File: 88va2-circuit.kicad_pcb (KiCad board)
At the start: 4 copper layers, 380 x 237.5 mm, 41 parts, among them CN2 FDD, CN4 TEXT BUS, CN5 LED, IC1 D65101GD055, IC13 SN74ALS374N, IC20 7407, IC21 uPD4990AC, IC22 DIP-14_W7.62mm, IC65 D65101GD110, IC9 D65200GD076, X2 32.768K

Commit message: wire power lines
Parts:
- added REF**: R_Array_SIP9, Resistor_THT:R_Array_SIP9, F.Cu at (83.5, 27.9)
- moved R18 2.35 mm to (98.7, 24.1)
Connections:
- IC1 pad 1: (no net) -> +5V
- IC1 pad 40: (no net) -> +5V
- IC1 pad 41: (no net) -> GND
- IC1 pad 42: (no net) -> GND
- IC1 pad 80: GND -> (no net)
- IC1 pad 81: +5V -> (no net)
- IC9 pad 1: (no net) -> +5V
- IC9 pad 41: (no net) -> GND
- IC9 pad 42: (no net) -> GND
- IC9 pad 79: GND -> (no net)
- IC9 pad 80: GND -> (no net)
- IC9 pad 81: +5V -> (no net)
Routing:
- net +5V: track 856.7 -> 1129.3 mm, vias 3 -> 6
- net GND: track 1260.7 -> 1372.7 mm, vias 10 -> 12
- net Net-(IC13-8D): track 54.2 -> 51.9 mm

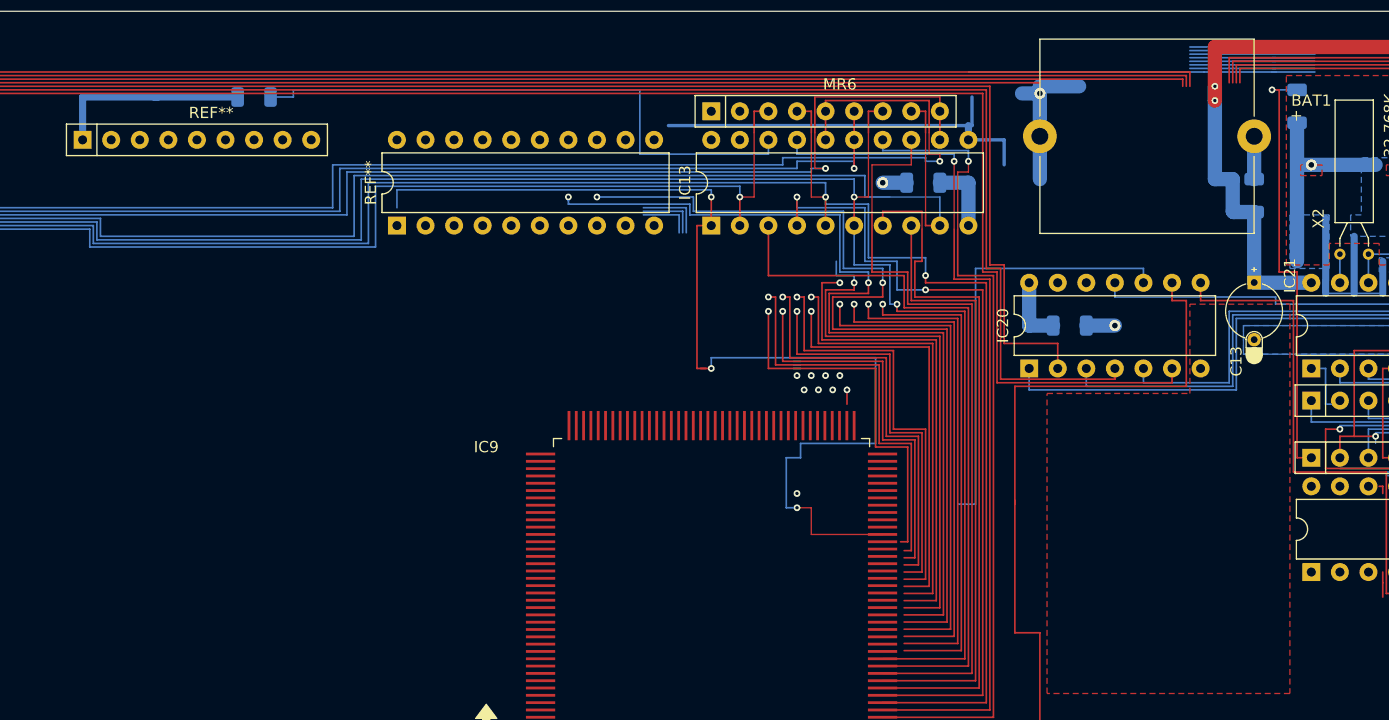
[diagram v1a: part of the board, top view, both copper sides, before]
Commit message: wire IC8, MR3
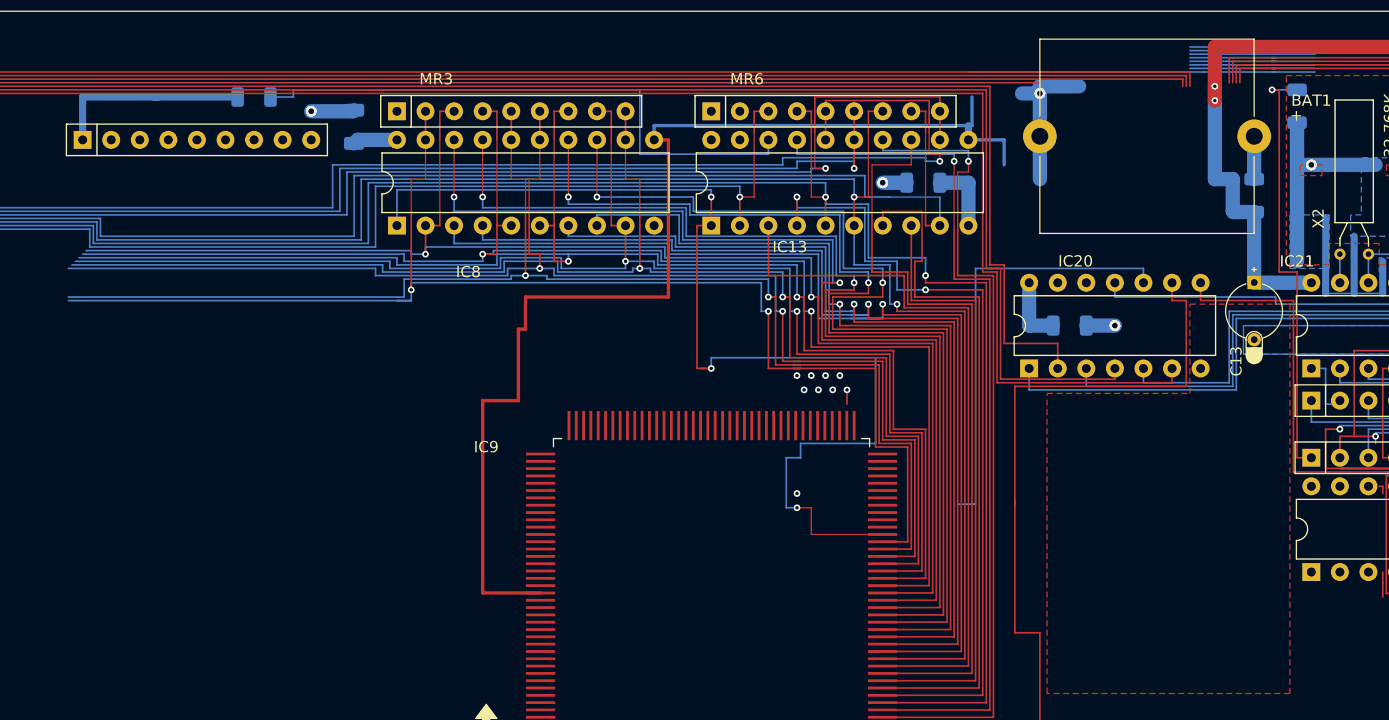
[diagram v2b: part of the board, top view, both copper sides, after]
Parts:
- removed the REF** at (111.4, 35.5)
- added C44: C_Small, Capacitor_SMD:C_1206_3216Metric, B.Cu at (107.6, 26.8)
- added IC8: SN74ALS374N, Package_DIP:DIP-20_W7.62mm, F.Cu at (111.4, 35.5)
- added MR3: 33kΩ, Resistor_THT:R_Array_SIP9, F.Cu at (111.4, 25.4)
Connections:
- IC9 pad 53: (no net) -> Net-(IC8-1D)
- IC9 pad 54: (no net) -> Net-(IC8-2D)
- IC9 pad 55: (no net) -> Net-(IC8-3D)
- IC9 pad 56: (no net) -> Net-(IC8-4D)
- IC9 pad 57: (no net) -> Net-(IC8-5D)
- IC9 pad 58: (no net) -> Net-(IC8-6D)
- IC9 pad 59: (no net) -> Net-(IC8-7D)
- IC9 pad 60: (no net) -> Net-(IC8-8D)
- IC9 pad 61: (no net) -> SCLK0
- IC9 pad 62: (no net) -> SCLK1
- IC9 pad 63: (no net) -> SCLK2
- IC9 pad 64: (no net) -> SCLK3
- IC9 pad 65: (no net) -> SCLK4
- IC9 pad 66: (no net) -> SCLK5
- IC9 pad 67: (no net) -> SCLK6
- IC9 pad 68: (no net) -> SCLK7
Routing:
- net (no net): track 2451.6 -> 1717.7 mm, vias 60 -> 42
- net SCLK1: track 0.00 -> 127.3 mm, vias 0 -> 2
- net SCLK2: track 0.00 -> 127.3 mm, vias 0 -> 2
- net SCLK0: track 0.00 -> 126.7 mm, vias 0 -> 2
- net SCLK3: track 0.00 -> 125.3 mm, vias 0 -> 2
- net SCLK4: track 0.00 -> 122.8 mm, vias 0 -> 2
- net SCLK5: track 0.00 -> 120.9 mm, vias 0 -> 2
- net SCLK7: track 0.00 -> 119.9 mm, vias 0 -> 2
- net SCLK6: track 0.00 -> 119.6 mm, vias 0 -> 2
- net Net-(IC8-1D): track 0.00 -> 95.3 mm, vias 0 -> 1
- net Net-(IC8-7D): track 0.00 -> 92.4 mm, vias 0 -> 2
- net Net-(IC8-8D): track 0.00 -> 91.7 mm, vias 0 -> 2
- net Net-(IC8-2D): track 0.00 -> 89.6 mm, vias 0 -> 1
- net Net-(IC8-5D): track 0.00 -> 88.6 mm, vias 0 -> 2
- net Net-(IC8-6D): track 0.00 -> 88.3 mm, vias 0 -> 2
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
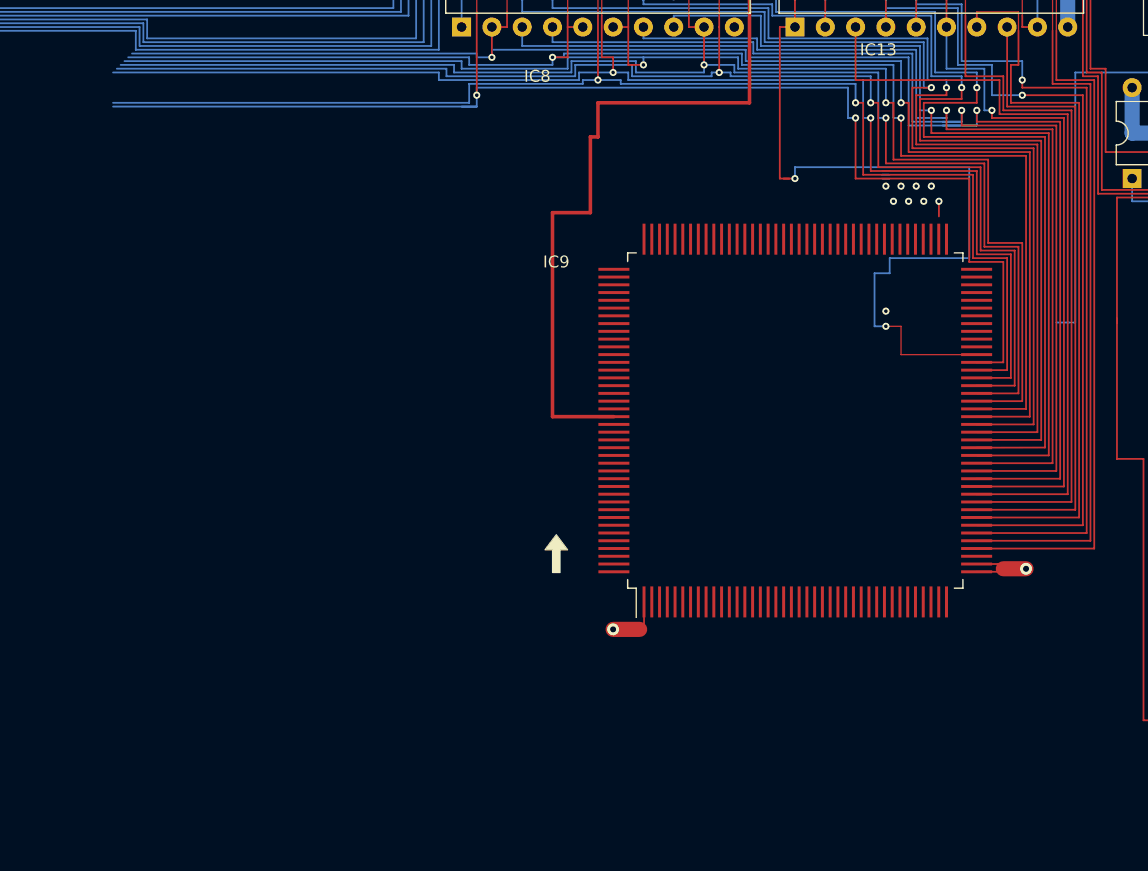
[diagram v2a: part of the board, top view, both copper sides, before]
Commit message: wire IC13/IC8 CLK
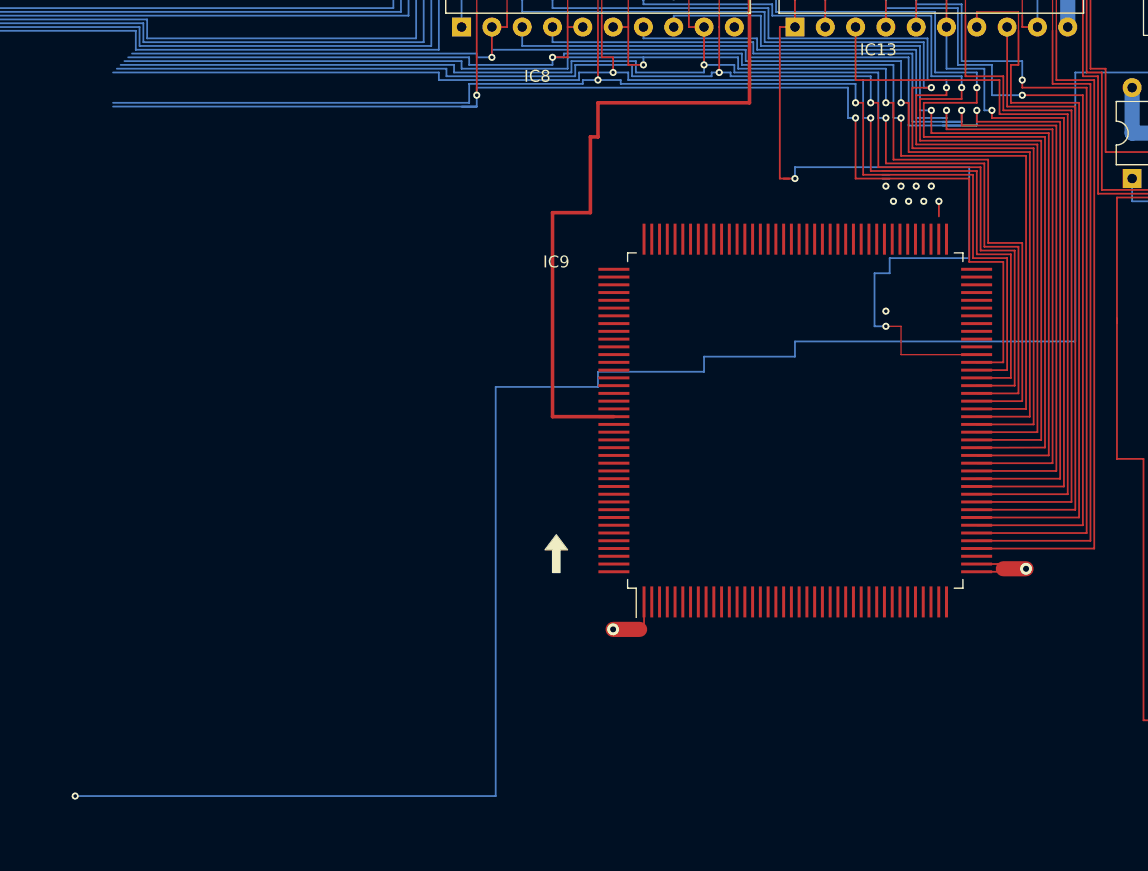
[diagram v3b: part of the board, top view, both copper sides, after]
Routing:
- net FDD_STEP: track 38.7 -> 160.7 mm, vias 0 -> 1
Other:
- board text added: "R116"
- board text added: "R117"
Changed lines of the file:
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@@
+    (effects (font (size 1 1) (thickness 0.1)) (justify left bottom mirror))
+  )
+  (gr_text "R116" (at 73.6125 98.0975 90) (layer "B.SilkS")
+    (effects (font (size 1 1) (thickness 0.1)) (justify left bottom mirror))
+  )
+  (gr_text "R117" (at 77.105 98.0975 90) (layer "B.SilkS")
     (effects (font (size 1 1) (thickness 0.1)) (justify left bottom mirror))
   )
@@
   (segment (start 51.705 23.8025) (end 51.07 24.4375) (width 0.15) (layer "F.Cu") (net 34))
   (segment (start 180.2925 48.25) (end 180.2925 49.52) (width 0.15) (layer "F.Cu") (net 34))
+  (via (at 79.01 100.0025) (size 0.6) (drill 0.3) (layers "F.Cu" "B.Cu") (net 37))
+  (segment (start 177.7525 40.63) (end 177.7525 39.36) (width 0.15) (layer "B.Cu") (net 37))
+  (segment (start 139.335 63.1725) (end 131.715 63.1725) (width 0.15) (layer "B.Cu") (net 37))
+  (segment (start 139.335 61.9025) (end 139.335 63.1725) (width 0.15) (layer "B.Cu") (net 37))
+  (segment (start 122.825 64.4425) (end 122.825 65.7125) (width 0.15) (layer "B.Cu") (net 37))
+  (segment (start 114.2525 100.0025) (end 79.01 100.0025) (width 0.15) (layer "B.Cu") (net 37))
   (segment (start 177.7525 39.36) (end 162.83 39.36) (width 0.15) (layer "B.Cu") (net 37))
-  (segment (start 162.83 39.36) (end 162.83 60.315) (width 0.15) (layer "B.Cu") (net 37))
-  (segment (start 177.7525 40.63) (end 177.7525 39.36) (width 0.15) (layer "B.Cu") (net 37))
-  (segment (start 162.83 60.315) (end 161.2425 60.315) (width 0.15) (layer "B.Cu") (net 37))
+  (segment (start 131.715 64.4425) (end 122.825 64.4425) (width 0.15) (layer "B.Cu") (net 37))
+  (segment (start 114.2525 65.7125) (end 114.2525 100.0025) (width 0.15) (layer "B.Cu") (net 37))
+  (segment (start 131.715 63.1725) (end 131.715 64.4425) (width 0.15) (layer "B.Cu") (net 37))
+  (segment (start 162.83 39.36) (end 162.83 61.9025) (width 0.15) (layer "B.Cu") (net 37))
+  (segment (start 162.83 61.9025) (end 139.335 61.9025) (width 0.15) (layer "B.Cu") (net 37))
+  (segment (start 122.825 65.7125) (end 114.2525 65.7125) (width 0.15) (layer "B.Cu") (net 37))
   (via (at 220.615 41.9) (size 0.6) (drill 0.3) (layers "F.Cu" "B.Cu") (net 38))
   (segment (start 189.5 42.535) (end 189.5 41.9) (width 0.15) (layer "B.Cu") (net 38))

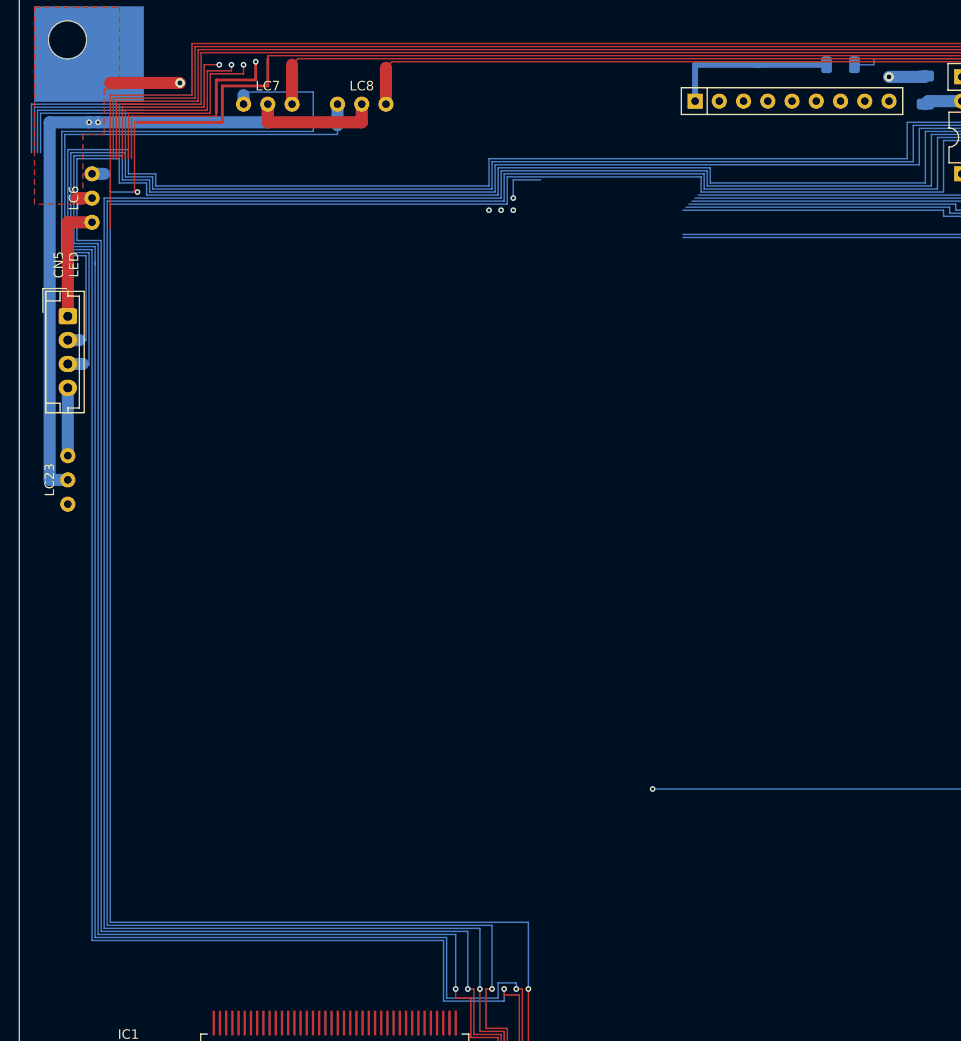
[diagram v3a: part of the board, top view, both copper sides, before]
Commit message: add GVRAM
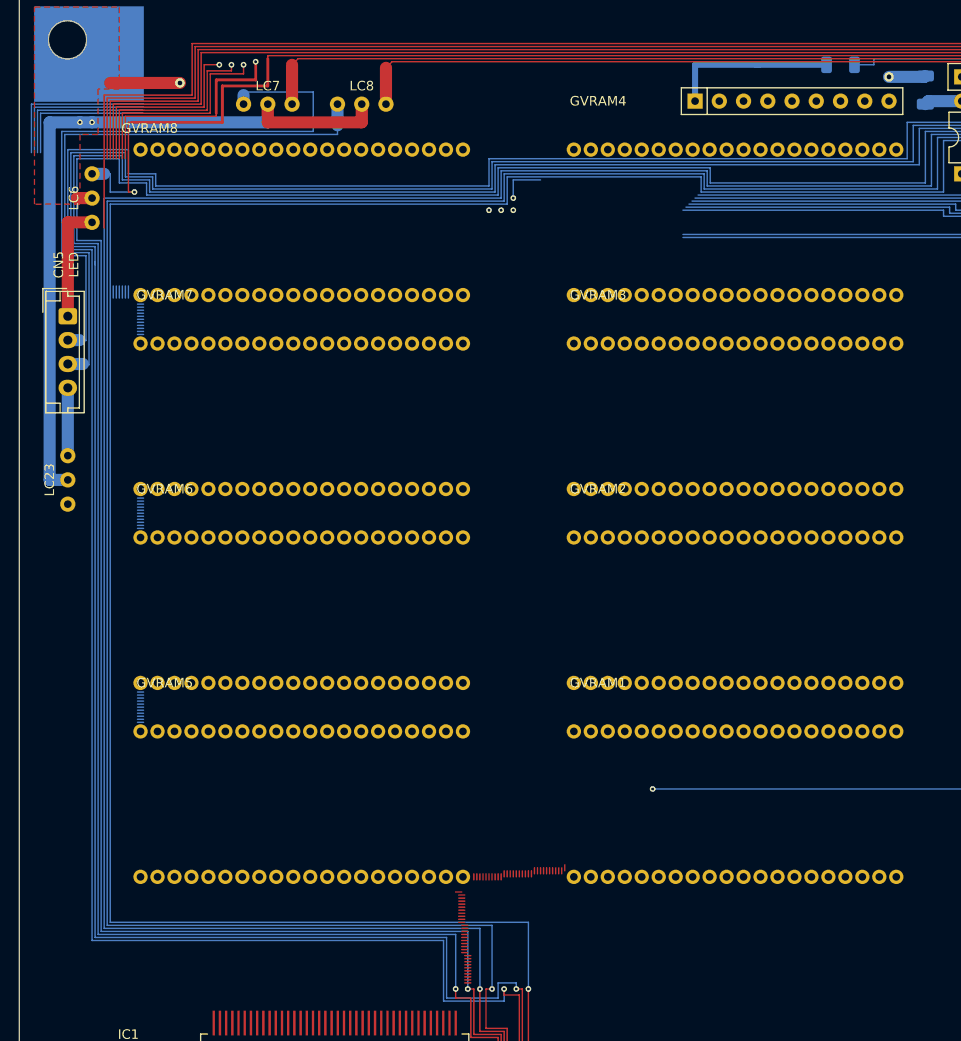
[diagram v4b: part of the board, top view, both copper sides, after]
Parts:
- added GVRAM1: D42233CU-15, 88va_Library:uPD42233CU, F.Cu at (70.8, 109.2)
- added GVRAM2: D42233CU-15, 88va_Library:uPD42233CU, F.Cu at (70.8, 88.9)
- added GVRAM3: D42233CU-15, 88va_Library:uPD42233CU, F.Cu at (70.8, 68.6)
- added GVRAM4: D42233CU-15, 88va_Library:uPD42233CU, F.Cu at (70.8, 48.2)
- added GVRAM5: D42233CU-15, 88va_Library:uPD42233CU, F.Cu at (25.4, 109.2)
- added GVRAM6: D42233CU-15, 88va_Library:uPD42233CU, F.Cu at (25.4, 88.9)
- added GVRAM7: D42233CU-15, 88va_Library:uPD42233CU, F.Cu at (25.4, 68.6)
- added GVRAM8: D42233CU-15, 88va_Library:uPD42233CU, F.Cu at (25.4, 48.2)
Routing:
- net (no net): track 1717.7 -> 1790.7 mm
- net Net-(IC20-Pad2): track 191.8 -> 192.4 mm

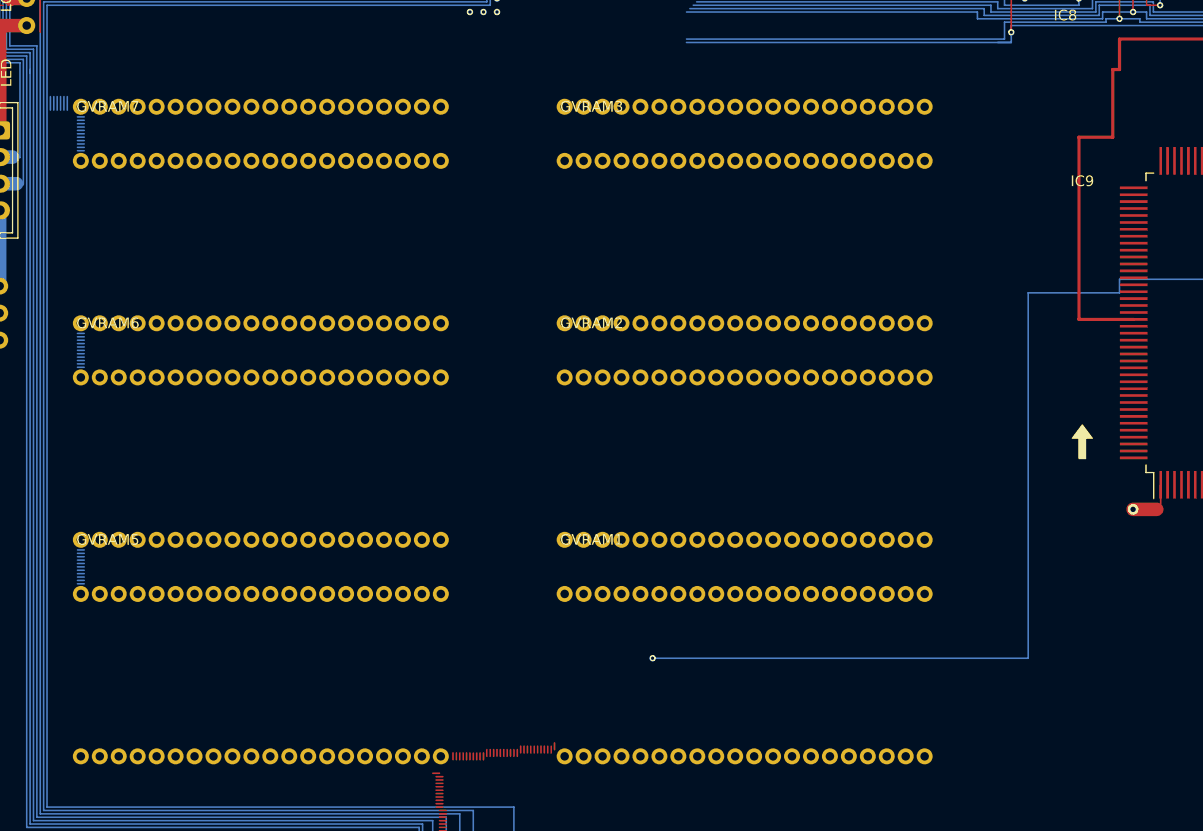
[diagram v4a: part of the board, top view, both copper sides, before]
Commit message: add GVRAM footprints
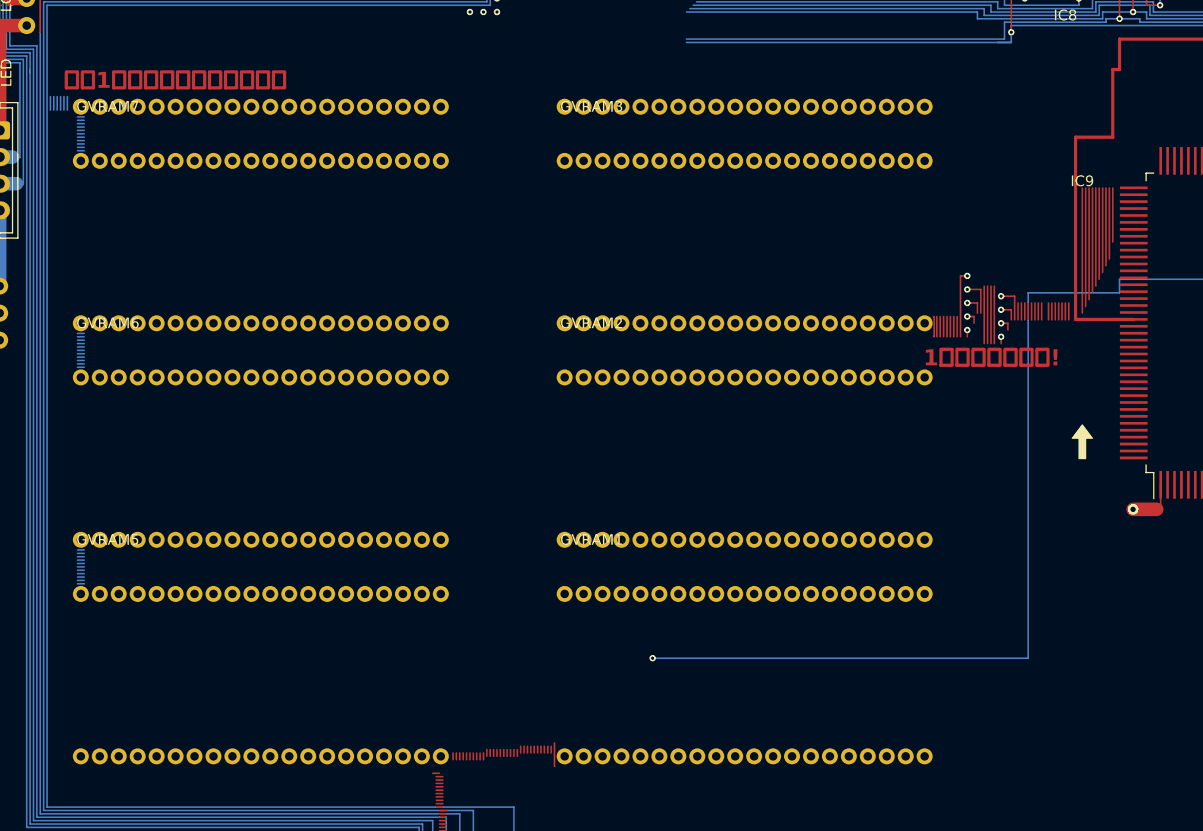
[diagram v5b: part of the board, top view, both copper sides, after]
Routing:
- net (no net): track 1790.7 -> 1961.9 mm, vias 42 -> 51
- net Net-(IC13-CLK): track 101.9 -> 102.6 mm
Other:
- board text added: "1ライン入らない!"
- board text added: "もう1グリッド左に寄せたい！"
